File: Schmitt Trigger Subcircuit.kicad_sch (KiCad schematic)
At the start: 5 parts, among them J1 Screw_Terminal_01x03, J2 Screw_Terminal_01x03, J3 Screw_Terminal_01x03, J4 Screw_Terminal_01x03, U1 74LV14

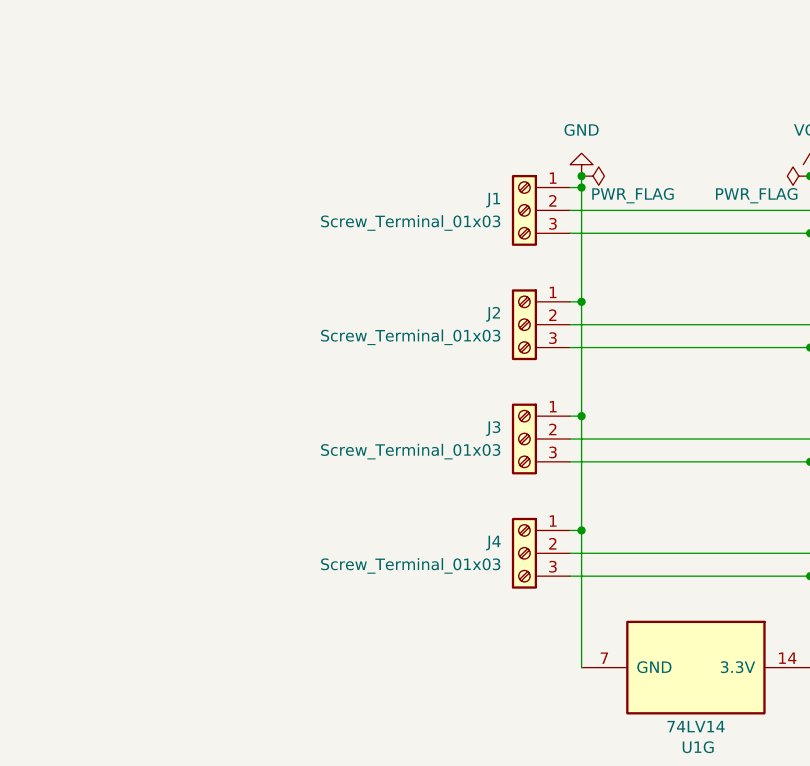
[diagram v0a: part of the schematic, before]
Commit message: Schmitt Trigger Subcircuit
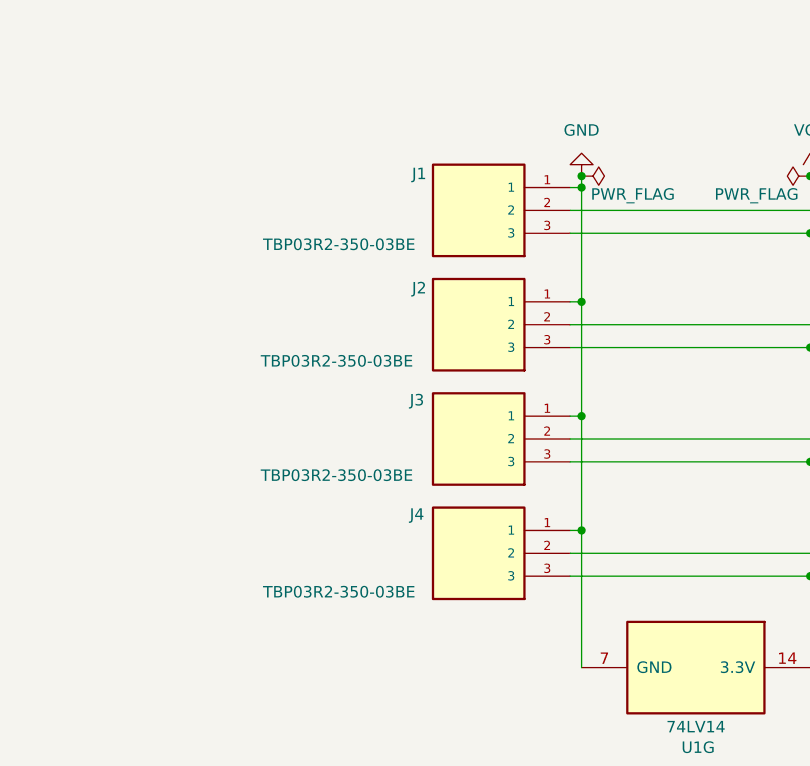
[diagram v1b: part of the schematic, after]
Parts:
- removed J1, J2, J3, J4: Screw_Terminal_01x03, TerminalBlock_4Ucon:TerminalBlock_4Ucon_1x03_P3.50mm_Horizontal, symbol Connector:Screw_Terminal_01x03
- added J1, J2, J3, J4: TBP03R2-350-03BE, TBP03R2_350_03BE:CUI_TBP03R2-350-03BE, symbol TBP03R2-350-03BE:TBP03R2-350-03BE
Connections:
- net GND: now also J1.1, J2.1, J3.1, J4.1
- net VCC: now also J1.3, J2.3, J3.3, J4.3
- net at U1.3: now also J2.2
- net at U1.1: now also J1.2
- net at U1.5: now also J3.2
- net at U1.9: now also J4.2
